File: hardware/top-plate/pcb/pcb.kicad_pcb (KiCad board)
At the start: 2 copper layers, 130 x 130 mm, 104 parts, among them J1 Conn_01x02, SW1 SS-12D10L5, SW2 TS4535TP 250GF 009, SW3 TS4535TP 250GF 009

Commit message: cleanup
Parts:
- moved H19 4.24 mm to (-35.0, -16.0)
- moved H20 4.24 mm to (35.0, -16.0)
- moved H23 2.83 mm to (-32.0, -29.0)
- moved H24 2.83 mm to (32.0, -29.0)
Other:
- outline, holes or cut-outs redrawn
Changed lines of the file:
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@@
 	(footprint "MountingHole:MountingHole_2.2mm_M2_Pad_Via"
 		(layer "F.Cu")
-		(at 34 -27)
+		(at 32 -29)
 		(descr "Mounting Hole 2.2mm, M2")
 		(tags "mounting hole 2.2mm m2")
@@
 	(footprint "MountingHole:MountingHole_2.2mm_M2_Pad_Via"
 		(layer "F.Cu")
-		(at -34 -27)
+		(at -32 -29)
 		(descr "Mounting Hole 2.2mm, M2")
 		(tags "mounting hole 2.2mm m2")
@@
 	(footprint "MountingHole:MountingHole_2.2mm_M2_Pad_Via"
 		(layer "F.Cu")
-		(at 32 -19)
+		(at 35 -16)
 		(descr "Mounting Hole 2.2mm, M2")
 		(tags "mounting hole 2.2mm m2")
@@
 	(footprint "MountingHole:MountingHole_2.2mm_M2_Pad_Via"
 		(layer "F.Cu")
-		(at -32 -19)
+		(at -35 -16)
 		(descr "Mounting Hole 2.2mm, M2")
 		(tags "mounting hole 2.2mm m2")
@@
 	(gr_rect
 		(start 16 -38)
-		(end 30 -24)
+		(end 28 -24)
 		(stroke
 			(width 0.2)
@@
 	)
 	(gr_rect
-		(start -32 16)
-		(end -24 26)
+		(start -32 13)
+		(end -24 25)
 		(stroke
 			(width 0.2)
@@
 	)
 	(gr_text "Team BotByWire\nTop PCB V0.1"
-		(at 35.8 -10.2 0)
+		(at 37.6 -7.6 0)
 		(layer "F.SilkS")
 		(effects

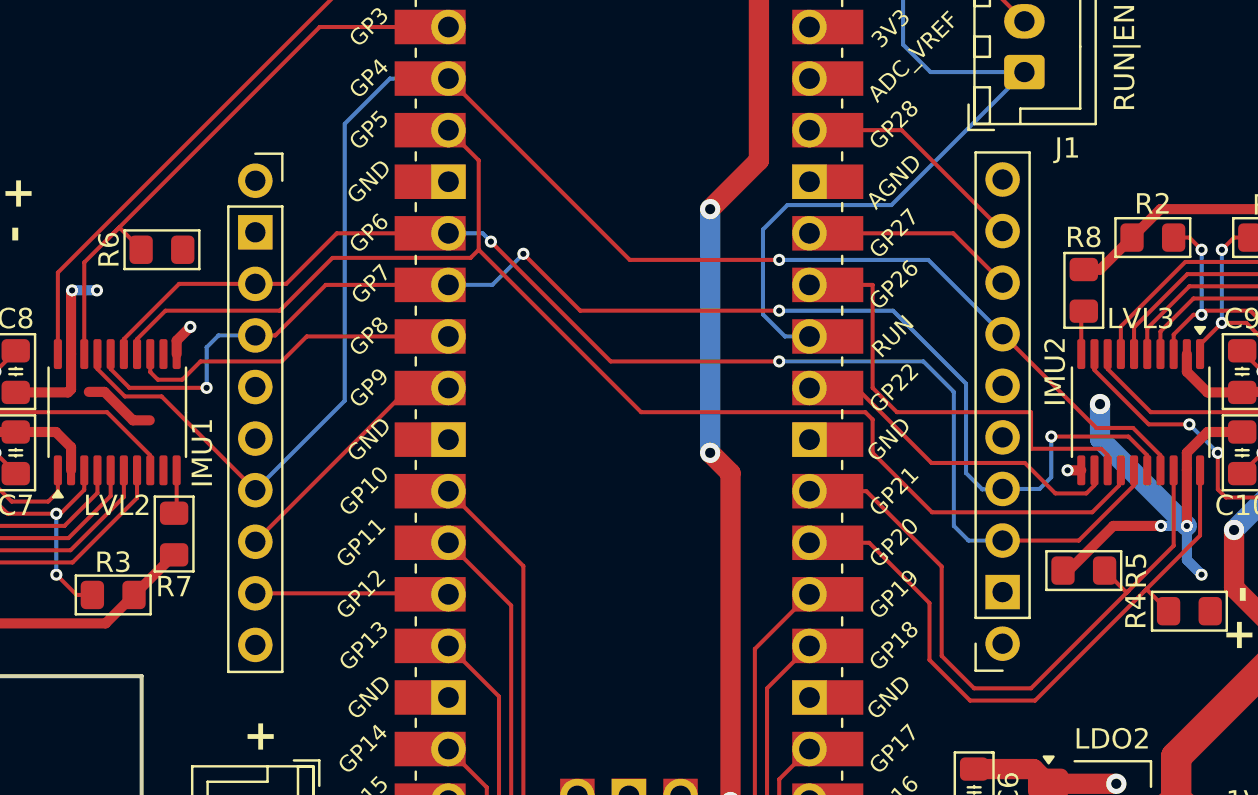
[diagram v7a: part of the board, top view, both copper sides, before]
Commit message: fixed icm20948 footprint (header positions were a tiny bit off)
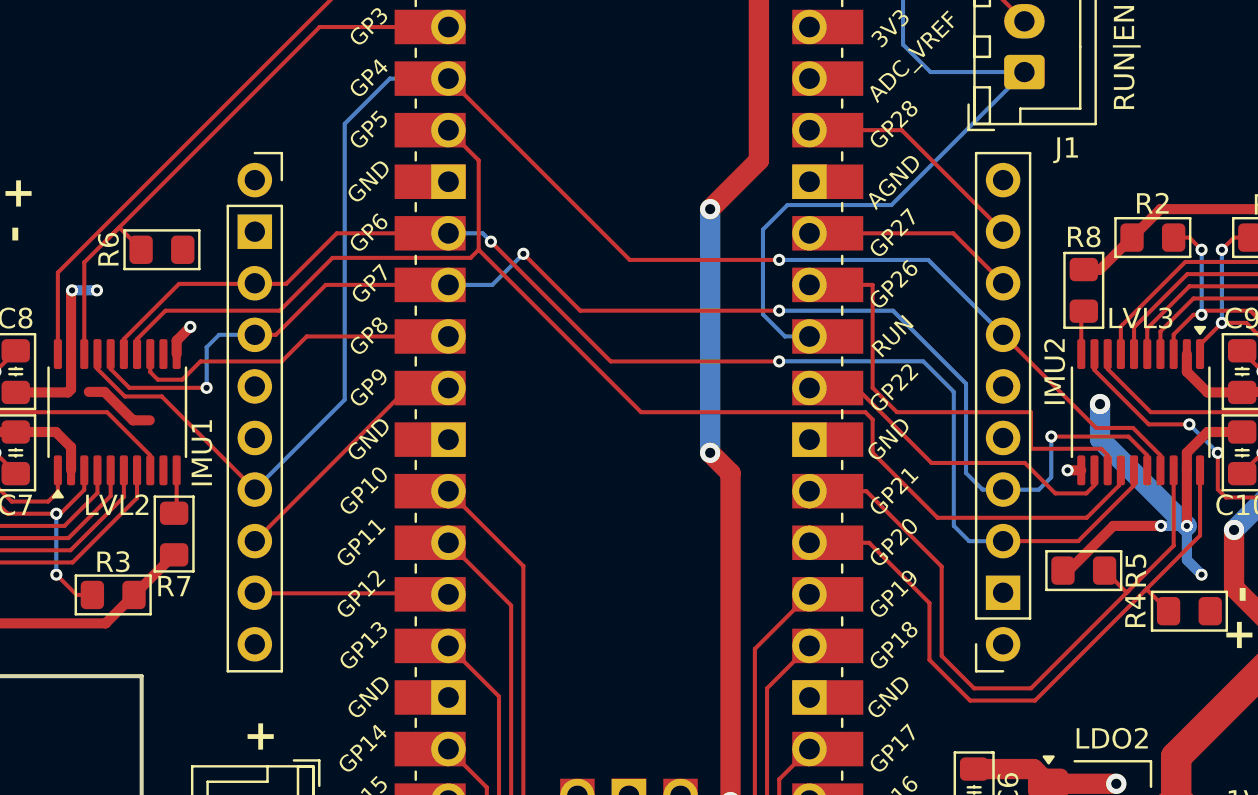
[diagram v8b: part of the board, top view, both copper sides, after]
